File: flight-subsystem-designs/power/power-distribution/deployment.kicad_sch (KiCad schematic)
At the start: 16 parts, among them J11 Conn_01x02, J12 Conn_01x02, Q3 BC848ALT1G, Q4 IRLML2803PBFCT, Q5 IRLML2803PBFCT

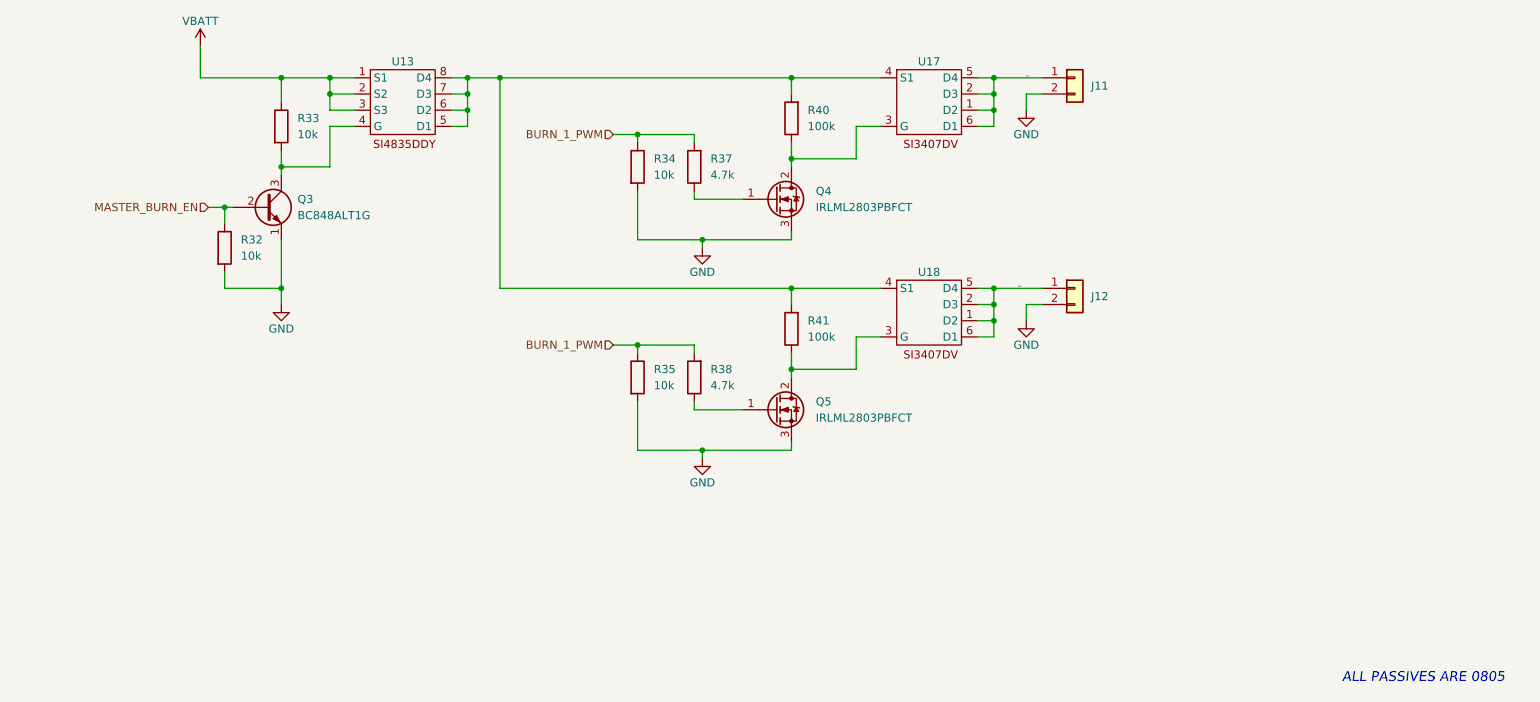
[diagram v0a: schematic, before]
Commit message: feat: PDU 4.0.0 (WIP)
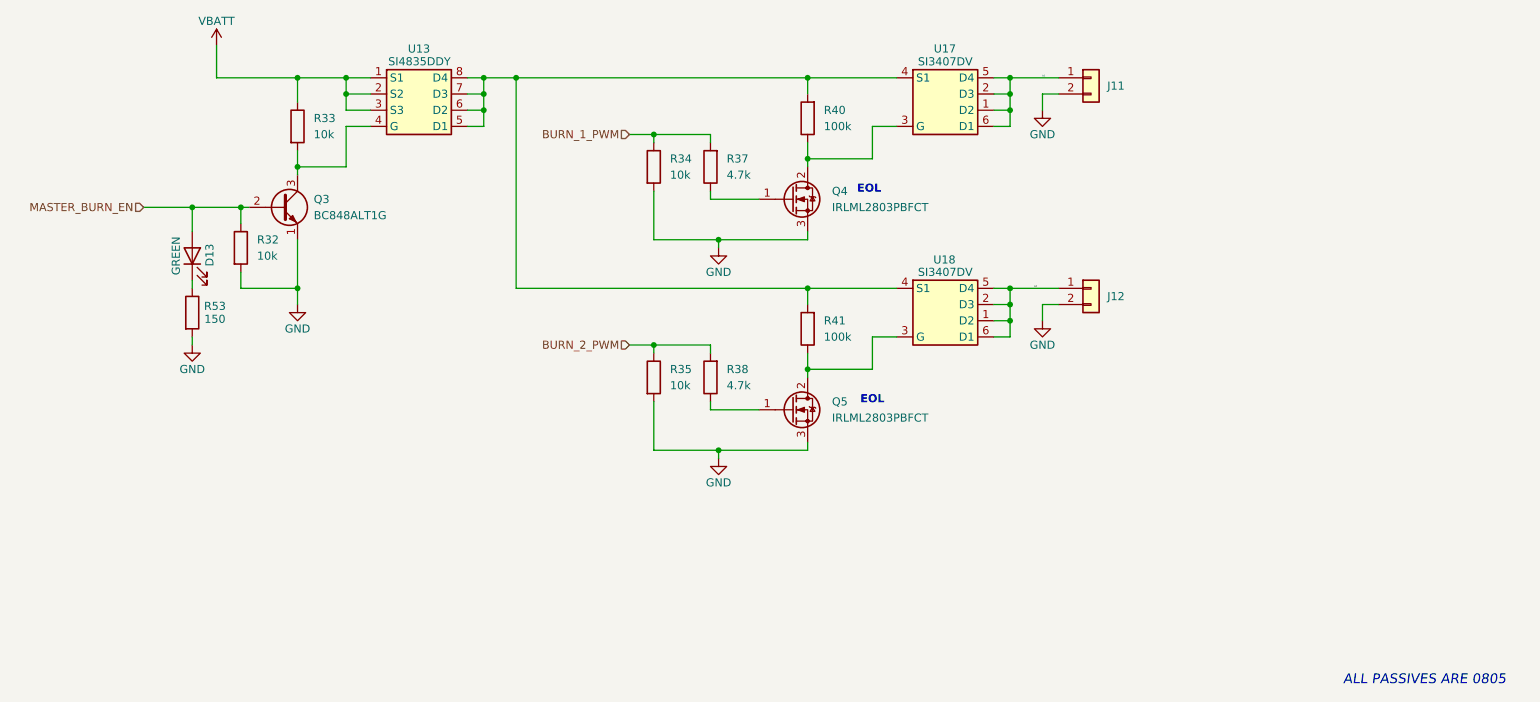
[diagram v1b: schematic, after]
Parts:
- added D13: GREEN, LED_SMD:LED_0603_1608Metric, symbol Device:LED
- added R53: 150, Resistor_SMD:R_0603_1608Metric, symbol Device:R
- U13: value ~ -> SI4835DDY
- U17, U18: value ~ -> SI3407DV
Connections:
- net BURN_1_PWM: no longer R35.1, R38.2
- net GND: now also R53.2
- net MASTER_BURN_EN: now also D13.2 (A)
- new net: D13.1 (K), R53.1
- new net BURN_2_PWM: R35.1, R38.2
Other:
- note added: "EOL"
- moved on the sheet: J11, J12, Q4, Q5, R32, R33, R34, R35, R37, R38, R40, R41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

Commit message: shi
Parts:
- J11, J12: footprint Connector_Molex:Molex_Pico-Lock_205338-0002_1x02-1MP_P2.00mm_Horizontal -> Connector_Molex:Molex_PicoBlade_53047-0210_1x02_P1.25mm_Vertical
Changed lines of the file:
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@@
 			)
 		)
-		(property "Footprint" "Connector_Molex:Molex_Pico-Lock_205338-0002_1x02-1MP_P2.00mm_Horizontal"
+		(property "Footprint" "Connector_Molex:Molex_PicoBlade_53047-0210_1x02_P1.25mm_Vertical"
 			(at 217.17 77.47 0)
 			(effects
@@
 			)
 		)
-		(property "Footprint" "Connector_Molex:Molex_Pico-Lock_205338-0002_1x02-1MP_P2.00mm_Horizontal"
+		(property "Footprint" "Connector_Molex:Molex_PicoBlade_53047-0210_1x02_P1.25mm_Vertical"
 			(at 217.17 110.49 0)
 			(effects
